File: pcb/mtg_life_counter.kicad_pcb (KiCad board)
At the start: 2 copper layers, 167.6 x 101.6 mm, 80 parts, among them J1 USB_C_Receptacle_USB2.0, J2 ICSP, SW1 SW_SPST, SW2 SW_SPST, U1 ATmega328P-AU, U2 74HC595, U3 74HC595, U4 TPIC6B595, U5 TPIC6B595, U6 74LS151, U7 FT232RL, Y1 16MHz

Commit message: complete electrical layout
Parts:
- removed the C10 at (67.5, 86.4)
- removed R4, R5: 1k, Resistor_SMD:R_0805_2012Metric_Pad1.15x1.40mm_HandSolder
- removed the U7 at (59.9, 89.8)
- added C5: 0.1uF, Capacitor_SMD:C_0805_2012Metric_Pad1.15x1.40mm_HandSolder, F.Cu at (177.8, 81.0)
- added C7: 0.1uF, Capacitor_SMD:C_0805_2012Metric_Pad1.15x1.40mm_HandSolder, F.Cu at (126.4, 122.2)
- added TP1: INT0, TestPoint:TestPoint_Pad_D1.0mm, B.Cu at (59.7, 90.2)
- added TP2: Debug, TestPoint:TestPoint_Pad_D1.0mm, B.Cu at (59.7, 85.1)
- added U3: 74HC595, Package_SO:SOIC-16_3.9x9.9mm_P1.27mm, F.Cu at (184.8, 82.5)
- added U5: 74HC595, Package_SO:SOIC-16_3.9x9.9mm_P1.27mm, F.Cu at (120.0, 120.7)
- D1: value KW4-56NX RED -> KW4-566CVB RED; footprint mtg_life_counter:KW4-56NX -> mtg_life_counter:KW4-566xxB_THT
- D2: value KW4-56NX GREEN -> KW4-566CVB GREEN; footprint mtg_life_counter:KW4-56NX -> mtg_life_counter:KW4-566xxB_THT
- D3: value KW4-56NX YELLOW -> KW4-566CVB YELLOW; footprint mtg_life_counter:KW4-56NX -> mtg_life_counter:KW4-566xxB_THT
- D4: value KW4-56NX BLUE -> KW4-566CVB BLUE; footprint mtg_life_counter:KW4-56NX -> mtg_life_counter:KW4-566xxB_THT
- moved C8 71.7 mm to (130.6, 62.9), turned to 0 degrees
- moved R2 69.5 mm to (130.6, 78.1), turned to 180 degrees
- moved C9 66.4 mm to (138.7, 141.0), turned to 180 degrees
- moved R3 61.1 mm to (138.7, 125.7), turned to 180 degrees
- moved U7 58.8 mm to (134.6, 133.3), turned to 180 degrees
- moved U6 58.6 mm to (134.6, 70.5), turned to 0 degrees
- moved U4 48.9 mm to (183.5, 120.7)
- moved C6 48.5 mm to (190.5, 122.2), turned to 270 degrees
- moved Y1 28.2 mm to (88.9, 111.8)
- moved SW1 27.9 mm to (63.5, 103.6)
- moved C10 23.6 mm to (81.3, 101.6), turned to 90 degrees
- moved C2 21.7 mm to (85.7, 109.2)
- moved C3 19.3 mm to (85.7, 111.1)
- moved C1 18.9 mm to (85.7, 107.3)
- moved E2 15.3 mm to (196.3, 66.1), turned to 0 degrees
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- renumbered C3 to C1, C9 to C10, C1 to C2, C4 to C3, C5 to C4, C7 to C8, C8 to C9, U3 to U4, U4 to U6, U5 to U7, U6 to U8
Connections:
- C1 pad 1: Net-(C3-Pad1) -> GND
- C1 pad 2: Net-(C3-Pad2) -> +5V
- C2 pad 1: Net-(C1-Pad1) -> GND
- C2 pad 2: Net-(C1-Pad2) -> +5V
- C3 pad 1: Net-(C4-Pad1) -> GND
- C3 pad 2: Net-(C4-Pad2) -> +5V
- E3 pad S1: /E3_SW -> GND
- E3 pad S2: GND -> /E3_SW
- E4 pad S1: /E4_SW -> GND
- E4 pad S2: GND -> /E4_SW
- J1 pad A6: /USB_D_P -> Net-(J1-PadA6)
- J1 pad A7: /USB_D_N -> Net-(J1-PadA7)
- J1 pad B6: /USB_D_P -> Net-(J1-PadB6)
- J1 pad B7: /USB_D_N -> Net-(J1-PadB7)
- J2 pad 3: /D13(SCK) -> /SER_CLK
- J2 pad 4: /D11(MOSI) -> /SER_DATA
- R10 pad 2: Net-(D1-Pad13) -> Net-(D1-Pad11)
- R11 pad 2: Net-(D1-Pad9) -> Net-(D1-Pad7)
- R15 pad 2: Net-(D1-Pad12) -> Net-(D1-Pad10)
- R20 pad 1: Net-(R10-Pad1) -> Net-(R20-Pad1)
- R20 pad 2: Net-(D2-Pad13) -> Net-(D2-Pad11)
- R21 pad 1: Net-(R11-Pad1) -> Net-(R21-Pad1)
- R21 pad 2: Net-(D2-Pad9) -> Net-(D2-Pad7)
- R22 pad 1: Net-(R12-Pad1) -> Net-(R22-Pad1)
- R23 pad 1: Net-(R13-Pad1) -> Net-(R23-Pad1)
- R24 pad 1: Net-(R14-Pad1) -> Net-(R24-Pad1)
- R25 pad 1: Net-(R15-Pad1) -> Net-(R25-Pad1)
- R25 pad 2: Net-(D2-Pad12) -> Net-(D2-Pad10)
- R26 pad 1: Net-(R16-Pad1) -> Net-(R26-Pad1)
- R27 pad 1: Net-(R17-Pad1) -> Net-(R27-Pad1)
- R30 pad 2: Net-(D3-Pad13) -> Net-(D3-Pad11)
- R31 pad 2: Net-(D3-Pad9) -> Net-(D3-Pad7)
- R35 pad 2: Net-(D3-Pad12) -> Net-(D3-Pad10)
- R40 pad 1: Net-(R30-Pad1) -> Net-(R40-Pad1)
- R40 pad 2: Net-(D4-Pad13) -> Net-(D4-Pad11)
- R41 pad 1: Net-(R31-Pad1) -> Net-(R41-Pad1)
- R41 pad 2: Net-(D4-Pad9) -> Net-(D4-Pad7)
- R42 pad 1: Net-(R32-Pad1) -> Net-(R42-Pad1)
- R43 pad 1: Net-(R33-Pad1) -> Net-(R43-Pad1)
- R44 pad 1: Net-(R34-Pad1) -> Net-(R44-Pad1)
- R45 pad 1: Net-(R35-Pad1) -> Net-(R45-Pad1)
- R45 pad 2: Net-(D4-Pad12) -> Net-(D4-Pad10)
- R46 pad 1: Net-(R36-Pad1) -> Net-(R46-Pad1)
- R47 pad 1: Net-(R37-Pad1) -> Net-(R47-Pad1)
- R50 pad 1: /E1_CLK -> /E1_DIR
- R51 pad 1: /E1_DIR -> /E1_CLK
- R52 pad 1: /E2_CLK -> /E2_DIR
- R53 pad 1: /E2_DIR -> /E2_CLK
- R54 pad 1: /E3_CLK -> /E3_DIR
- R55 pad 1: /E3_DIR -> /E3_CLK
- R56 pad 1: /E4_CLK -> /E4_DIR
- R57 pad 1: /E4_DIR -> /E4_CLK
- U1 pad 1: Net-(U1-Pad1) -> /RESET_BTN
- U1 pad 10: /MUX_SEL_2 -> /MUX_SEL_1
- U1 pad 11: /MUX_RB -> /MUX_SEL_0
- U1 pad 12: /~ENABLE -> /E3_SW
- U1 pad 16: Net-(U1-Pad16) -> /D12(MISO)
- U1 pad 2: /MUX_SEL_0 -> /E4_SW
- U1 pad 23: /E1_SW -> /ROLL_BTN
- U1 pad 25: /E3_SW -> /E1_SW
- U1 pad 26: /E4_SW -> /MUX_RB
- U1 pad 27: /ROLL_BTN -> Net-(U1-Pad27)
- U1 pad 28: /RESET_BTN -> /DEBUG_PIN
- U1 pad 32: Net-(U1-Pad32) -> /D2(INT0)
- U1 pad 9: /MUX_SEL_1 -> /MUX_SEL_2
- U2 pad 13: /~ENABLE -> GND
- U2 pad 14: /SER_LINK_3 -> /SER_LINK_5
- U4 pad 13: /~ENABLE -> GND
- U4 pad 14: /SER_LINK_2 -> /SER_LINK_3
- U4 pad 9: /SER_LINK_3 -> /SER_LINK_4
- U6 pad 14: Net-(D2-Pad14) -> Net-(D2-Pad12)
- U6 pad 15: Net-(D2-Pad11) -> Net-(D2-Pad9)
- U6 pad 16: Net-(D2-Pad10) -> Net-(D2-Pad8)
- U6 pad 4: Net-(D1-Pad14) -> Net-(D1-Pad12)
- U6 pad 5: Net-(D1-Pad11) -> Net-(D1-Pad9)
- U6 pad 6: Net-(D1-Pad10) -> Net-(D1-Pad8)
- U6 pad 9: /~ENABLE -> GND
- U7 pad 14: Net-(D4-Pad14) -> Net-(D4-Pad12)
- U7 pad 15: Net-(D4-Pad11) -> Net-(D4-Pad9)
- U7 pad 16: Net-(D4-Pad10) -> Net-(D4-Pad8)
- U7 pad 4: Net-(D3-Pad14) -> Net-(D3-Pad12)
- U7 pad 5: Net-(D3-Pad11) -> Net-(D3-Pad9)
- U7 pad 6: Net-(D3-Pad10) -> Net-(D3-Pad8)
- U7 pad 9: /~ENABLE -> GND
- U8 pad 1: /E2_DIR -> /E2_CLK
- U8 pad 12: /E4_DIR -> /E4_CLK
- U8 pad 13: /E4_CLK -> /E4_DIR
- U8 pad 14: /E3_DIR -> /E3_CLK
- U8 pad 15: /E3_CLK -> /E3_DIR
- U8 pad 2: /E2_CLK -> /E2_DIR
- U8 pad 3: /E1_DIR -> /E1_CLK
- U8 pad 4: /E1_CLK -> /E1_DIR
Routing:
- net +5V: track 281.0 -> 534.0 mm, vias 8 -> 24
- net /~ENABLE: track 245.8 -> 0.00 mm, vias 4 -> 0
- net Net-(D4-Pad10): track 120.7 -> 3.81 mm, vias 2 -> 0
- net Net-(D4-Pad14): track 115.6 -> 0.00 mm, vias 2 -> 0
- net Net-(D1-Pad10): track 116.8 -> 3.81 mm, vias 2 -> 0
- net Net-(D1-Pad11): track 113.0 -> 3.81 mm, vias 2 -> 0
- net Net-(D4-Pad11): track 111.8 -> 3.81 mm, vias 2 -> 0
- net Net-(D1-Pad14): track 104.1 -> 0.00 mm, vias 2 -> 0
- net Net-(D4-Pad6): track 102.7 -> 23.6 mm, vias 1 -> 0
- net /SER_LINK_5: track 0.00 -> 73.7 mm, vias 0 -> 2
- net Net-(R10-Pad1): track 81.7 -> 16.6 mm, vias 3 -> 2
- net Net-(D1-Pad6): track 109.0 -> 44.9 mm, vias 1 -> 2
- net Net-(R31-Pad1): track 83.0 -> 22.2 mm, vias 3 -> 2
- net Net-(R14-Pad1): track 80.3 -> 20.9 mm, vias 3 -> 2
- net Net-(R32-Pad1): track 84.3 -> 25.2 mm, vias 3 -> 2
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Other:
- board text added: "Serial"
- board text added: "TODO - Verify 7seg footprint - Verify TPIC footprint - Cosmetics - Check USB pin pitch - SMD LED version"

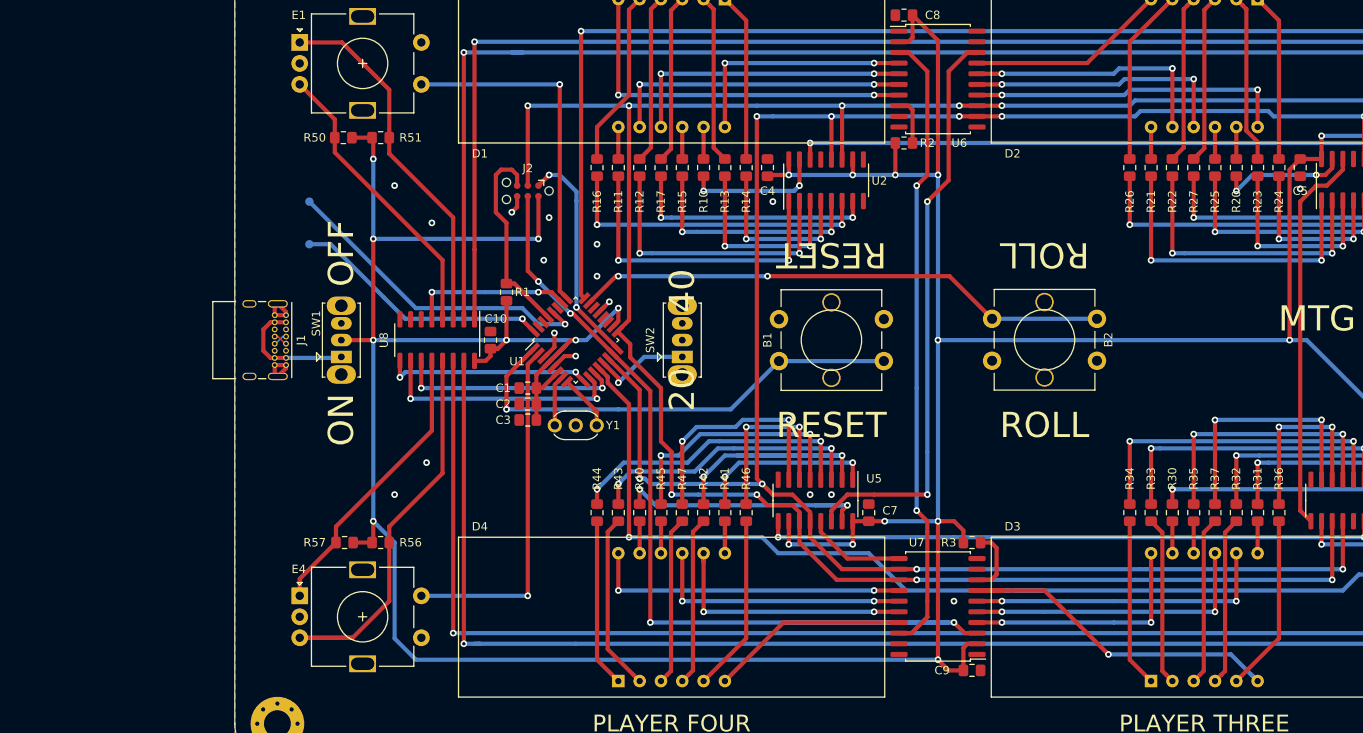
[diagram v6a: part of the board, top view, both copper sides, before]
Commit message: Switch to 74x165. Optimize pin assignments
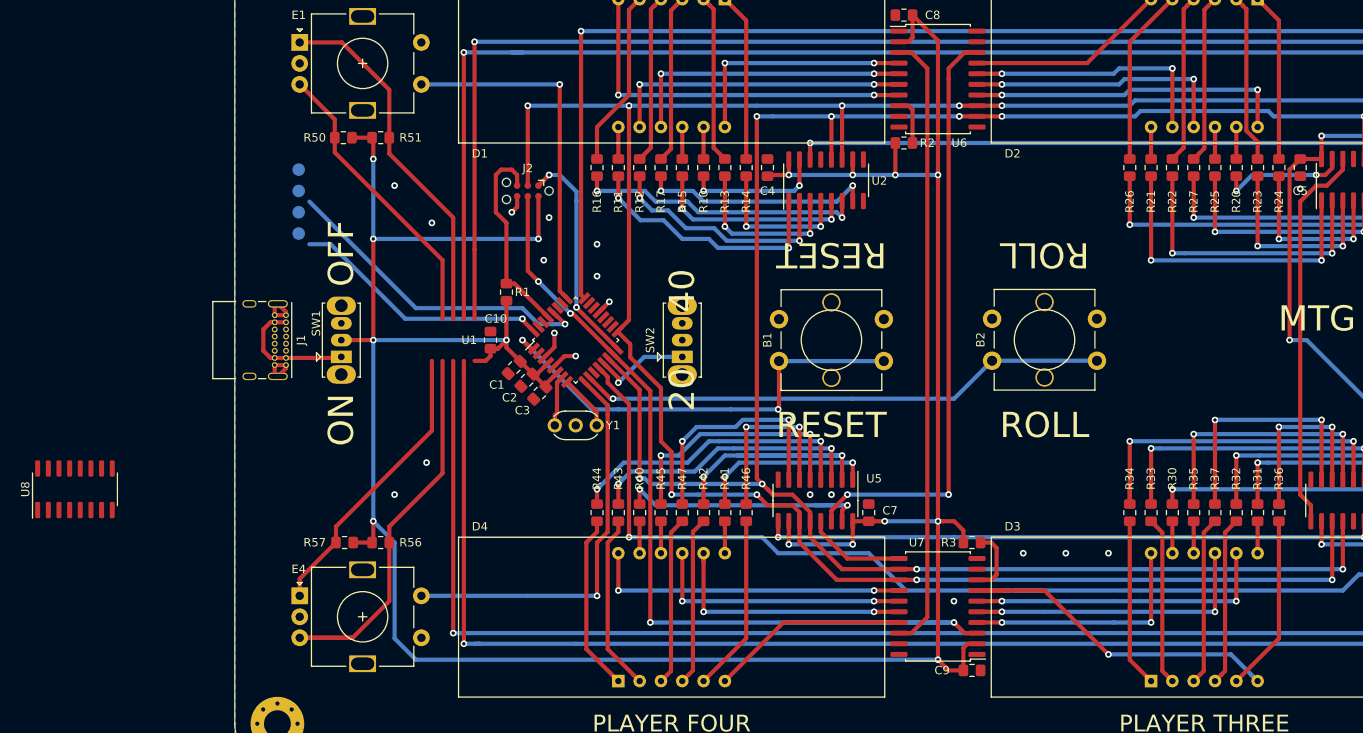
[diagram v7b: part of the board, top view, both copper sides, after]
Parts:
- added TP1: TX, TestPoint:TestPoint_Pad_D1.5mm, B.Cu at (58.4, 81.3)
- added TP2: RX, TestPoint:TestPoint_Pad_D1.5mm, B.Cu at (58.4, 83.8)
- TP3: renamed from TP1; footprint TestPoint:TestPoint_Pad_D1.0mm -> TestPoint:TestPoint_Pad_D1.5mm
- TP4: renamed from TP2; footprint TestPoint:TestPoint_Pad_D1.0mm -> TestPoint:TestPoint_Pad_D1.5mm
- U8: value 74LS151 -> 74HC165
- moved U8 46.7 mm to (31.8, 119.4), turned to 90 degrees
- moved C3 3.52 mm to (87.2, 107.9), turned to 45 degrees
- moved C1 2.93 mm to (84.1, 104.9), turned to 45 degrees
- moved C2 2.83 mm to (85.6, 106.4), turned to 45 degrees
- moved TP3 1.80 mm to (58.4, 88.9)
- moved TP4 1.80 mm to (58.4, 86.4)
- turned B2 to 0 degrees
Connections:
- net /D12(MISO) renamed /SER_MISO
- net /SER_DATA renamed /SER_MOSI
- U1 pad 10: /MUX_SEL_1 -> /ROLL_BTN
- U1 pad 11: /MUX_SEL_0 -> Net-(U1-Pad11)
- U1 pad 2: /E4_SW -> Net-(U1-Pad2)
- U1 pad 23: /ROLL_BTN -> Net-(U1-Pad23)
- U1 pad 26: /MUX_RB -> Net-(U1-Pad26)
- U1 pad 9: /MUX_SEL_2 -> /E4_SW
- U8 pad 1: /E2_CLK -> /SER_LATCH
- U8 pad 10: /MUX_SEL_1 -> GND
- U8 pad 11: /MUX_SEL_0 -> /E1_DIR
- U8 pad 12: /E4_CLK -> /E1_CLK
- U8 pad 13: /E4_DIR -> /E2_DIR
- U8 pad 14: /E3_CLK -> /E2_CLK
- U8 pad 15: /E3_DIR -> GND
- U8 pad 2: /E2_DIR -> /SER_CLK
- U8 pad 3: /E1_CLK -> /E3_DIR
- U8 pad 4: /E1_DIR -> /E3_CLK
- U8 pad 5: /MUX_RB -> /E4_DIR
- U8 pad 6: Net-(U8-Pad6) -> /E4_CLK
- U8 pad 7: GND -> Net-(U8-Pad7)
- U8 pad 9: /MUX_SEL_2 -> /SER_IN
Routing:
- net +5V: track 534.0 -> 468.8 mm, vias 24 -> 21
- net /MUX_SEL_1: track 29.7 -> 0.00 mm, vias 2 -> 0
- net /MUX_SEL_0: track 27.1 -> 0.00 mm, vias 2 -> 0
- net /MUX_SEL_2: track 24.8 -> 0.00 mm, vias 2 -> 0
- net /MUX_RB: track 19.3 -> 0.00 mm, vias 2 -> 0
- net Net-(R11-Pad1): track 37.4 -> 31.0 mm
- net /E4_SW: track 42.1 -> 48.1 mm
- net Net-(R12-Pad1): track 34.5 -> 28.5 mm
- net /RESET_BTN: track 58.8 -> 54.0 mm, vias 1 -> 2
- net Net-(R15-Pad1): track 28.1 -> 24.4 mm
- net Net-(R16-Pad1): track 37.8 -> 34.3 mm
- net Net-(R13-Pad1): track 23.9 -> 20.4 mm
- net Net-(R14-Pad1): track 20.9 -> 17.9 mm
- net /SER_LINK_1: track 76.4 -> 73.7 mm, vias 2 -> 0
- net Net-(R17-Pad1): track 29.8 -> 27.8 mm
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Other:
- rule via_min_size: 0.4 -> 0.6

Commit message: Finish routing
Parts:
- moved U8 47.9 mm to (76.2, 101.6)
- moved C10 11.4 mm to (69.8, 101.6), turned to 270 degrees
- moved J2 9.92 mm to (93.3, 90.2), turned to 90 degrees
- moved TP1 5.68 mm to (55.9, 86.4)
- moved TP4 5.68 mm to (55.9, 81.3)
- moved TP2 2.54 mm to (55.9, 83.8)
- moved TP3 2.54 mm to (55.9, 88.9)
- moved R1 2.27 mm to (85.0, 97.2), turned to 225 degrees
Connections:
- E2 pad S1: /E2_SW -> GND
- E2 pad S2: GND -> /E2_SW
- U1 pad 24: /E2_SW -> Net-(U1-Pad24)
- U1 pad 25: /E1_SW -> Net-(U1-Pad25)
- U1 pad 26: Net-(U1-Pad26) -> /E2_SW
- U1 pad 27: Net-(U1-Pad27) -> /E1_SW
- U8 pad 11: /E1_DIR -> /E2_CLK
- U8 pad 12: /E1_CLK -> /E2_DIR
- U8 pad 13: /E2_DIR -> /E1_CLK
- U8 pad 14: /E2_CLK -> /E1_DIR
- U8 pad 3: /E3_DIR -> /E4_CLK
- U8 pad 4: /E3_CLK -> /E4_DIR
- U8 pad 5: /E4_DIR -> /E3_CLK
- U8 pad 6: /E4_CLK -> /E3_DIR
- U8 pad 9: /SER_IN -> /SER_MISO
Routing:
- net +5V: track 468.8 -> 613.0 mm, vias 21 -> 17
- net /SER_LATCH: track 238.9 -> 279.7 mm, vias 9 -> 13
- net /D0(RX): track 0.00 -> 38.2 mm, vias 0 -> 1
- net /D1(TX): track 0.00 -> 36.8 mm, vias 0 -> 1
- net /SER_CLK: track 265.8 -> 298.6 mm, vias 10 -> 14
- net GND: track 32.0 -> 38.9 mm, vias 19 -> 25
- net /SER_MISO: track 26.6 -> 33.5 mm, vias 2 -> 4
- net /SER_MOSI: track 108.5 -> 113.6 mm, vias 4 -> 5
- net /DEBUG_PIN: track 38.6 -> 43.4 mm
- net /D2(INT0): track 31.2 -> 35.7 mm
- net /E4_CLK: track 34.5 -> 39.0 mm, vias 0 -> 2
- net Net-(D3-Pad6): track 42.0 -> 37.9 mm
- net /~RESET: track 24.4 -> 28.3 mm, vias 0 -> 2
- net /E1_DIR: track 35.1 -> 37.1 mm
- net /RESET_BTN: track 54.0 -> 52.1 mm
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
